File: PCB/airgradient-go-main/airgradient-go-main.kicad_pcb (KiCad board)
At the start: 4 copper layers, 62.9 x 88.3 mm, 192 parts, among them CN3 SM05B-SRSS-TB (LF)(SN), CN4 SM05B-SRSS-TB (LF)(SN), CN5 SM05B-SRSS-TB (LF)(SN), Q1 SIA445EDJ-T1-GE3, Q2 ZVN4106FTA_C508255, Q3 CSD83325L, Q4 SS8050-G, Q5 SI1308EDL, SW1 TS-1091C-A1B3-D2, SW2 TS-1091C-A1B3-D2, U1 W25N512GVEIG, U10 SGP41-D-R4, U11 PS1-CO-SMOKE-10k, U12 SHT4x, U13 SPL07-003, U14 LIS2DH12TR, U15 TMUX121NKGR_C22428404, U16 S12, U17 TCA6408ARGT, U18 TAU1113, U19 LM66200DRLR, U2 ZDSD512MLGEAG, U20 LP5036, U3 BQ27742YZFR-G1, U4 ESP32-C5-MINI-1, U5 BQ25628RYKR, U6 HYG-8503A, U7 TPL5010DDCR, U8 TPS63802DLAR, U9 TPS7A0228DQNR

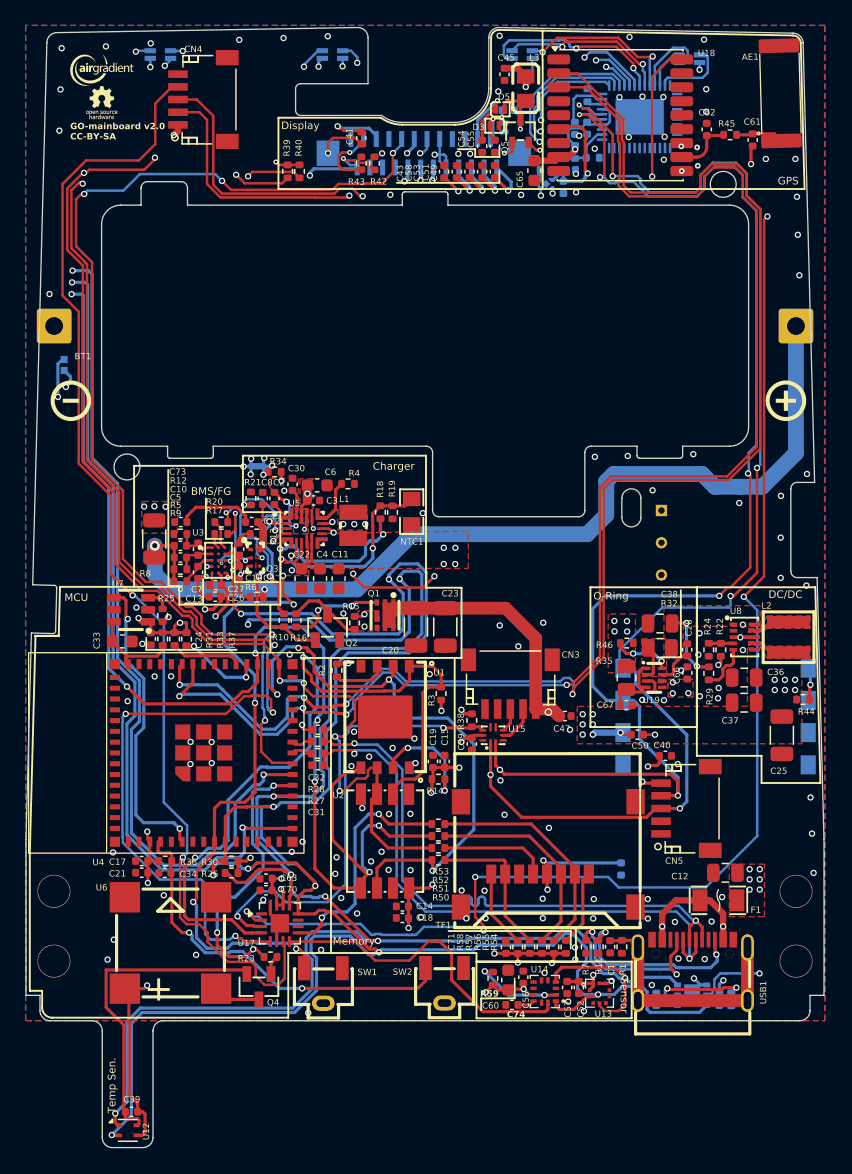
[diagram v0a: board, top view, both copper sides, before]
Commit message: Schematic: - Change SPI pull-ups R2/R3/R14 from 10K to 100K - Connect C74 decoupling cap to +3.1V rail (was floating)
PCB:
- Narrow the board outline around the temperature sensor area
- Move S12 0.3mm left and rework nearby I2C tracks
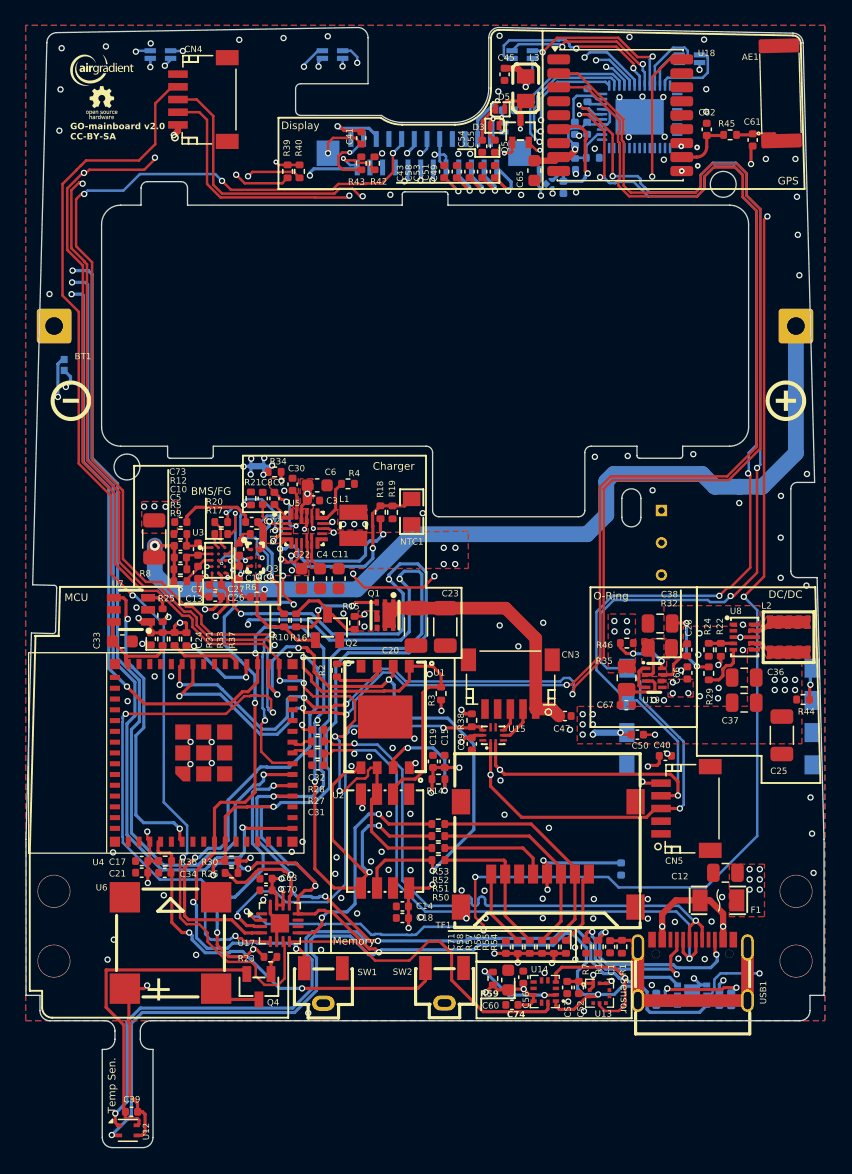
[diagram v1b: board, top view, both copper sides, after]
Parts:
- R14, R2, R3: value 10K -> 100K
- moved U16 0.30 mm to (155.6, 102.5)
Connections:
- C74 pad 2: Net-(U14-VDD_IO) -> +3.1V
- U14 pad 10: Net-(U14-VDD_IO) -> +3.1V
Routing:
- net /SCL: track 350.2 -> 353.9 mm
- net +3.1V: track 116.9 -> 118.7 mm
- net Net-(U14-VDD_IO): track 1.35 -> 0.00 mm
- net /SDA: track 341.5 -> 340.1 mm
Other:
- outline, holes or cut-outs redrawn

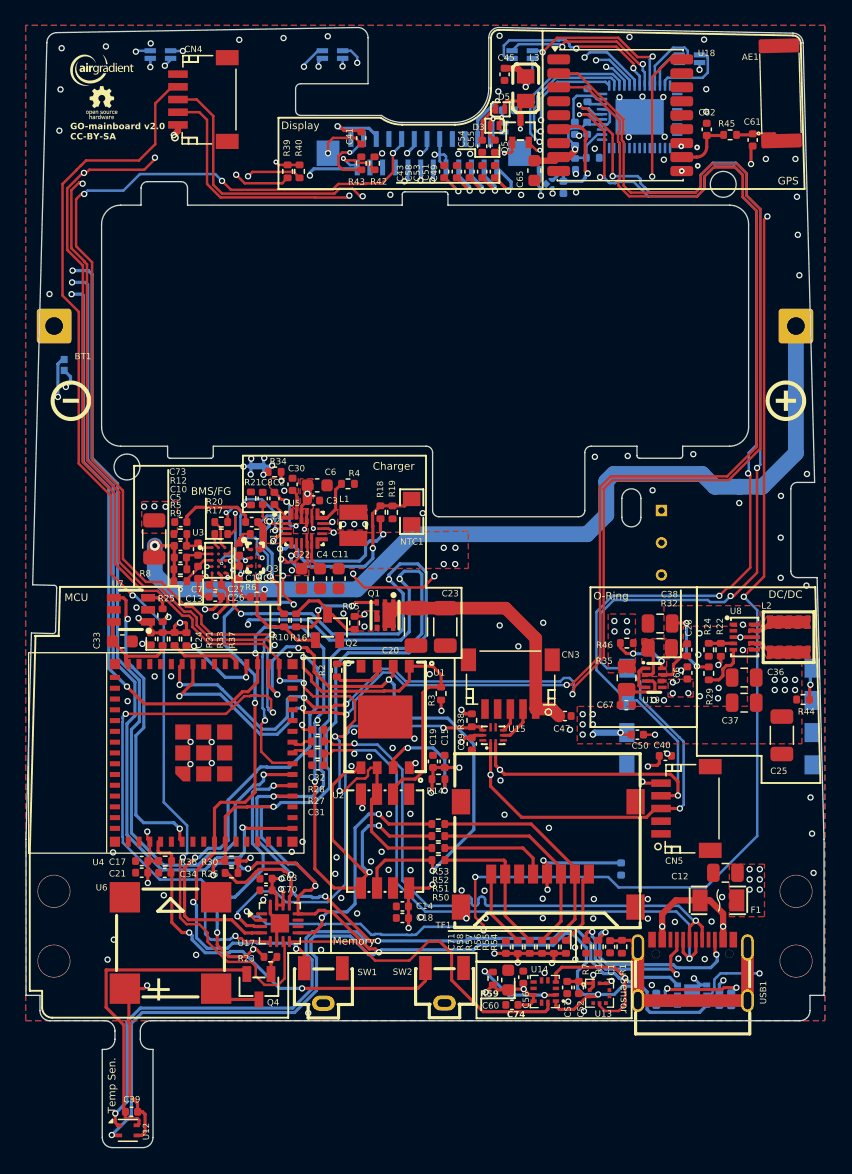
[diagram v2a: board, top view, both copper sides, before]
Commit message: v2.1: post-prototype fixes from v2.0 review and issue #1
- Battery: add C75 (100nF 0402) from BAT+ to GND at the battery +
  terminal as an RF shunt, with a GND via next to it
- NTC1 moved next to the battery negative tab (B.Cu), part changed
  to NCP15XH103F03RC; BQ25628 TS divider R18/R19 = 5.23k/30.1k
- Add R60 100K pull-up on TCA6408 RESET
- BOM: fix LCSC part numbers that were shared across different values
  (R13 2K -> C4109, R5/R12 200R -> C25087, 100K group -> C60491,
  C17/C21/C27 corrected)
- Remove test point footprints that were placed outside the board
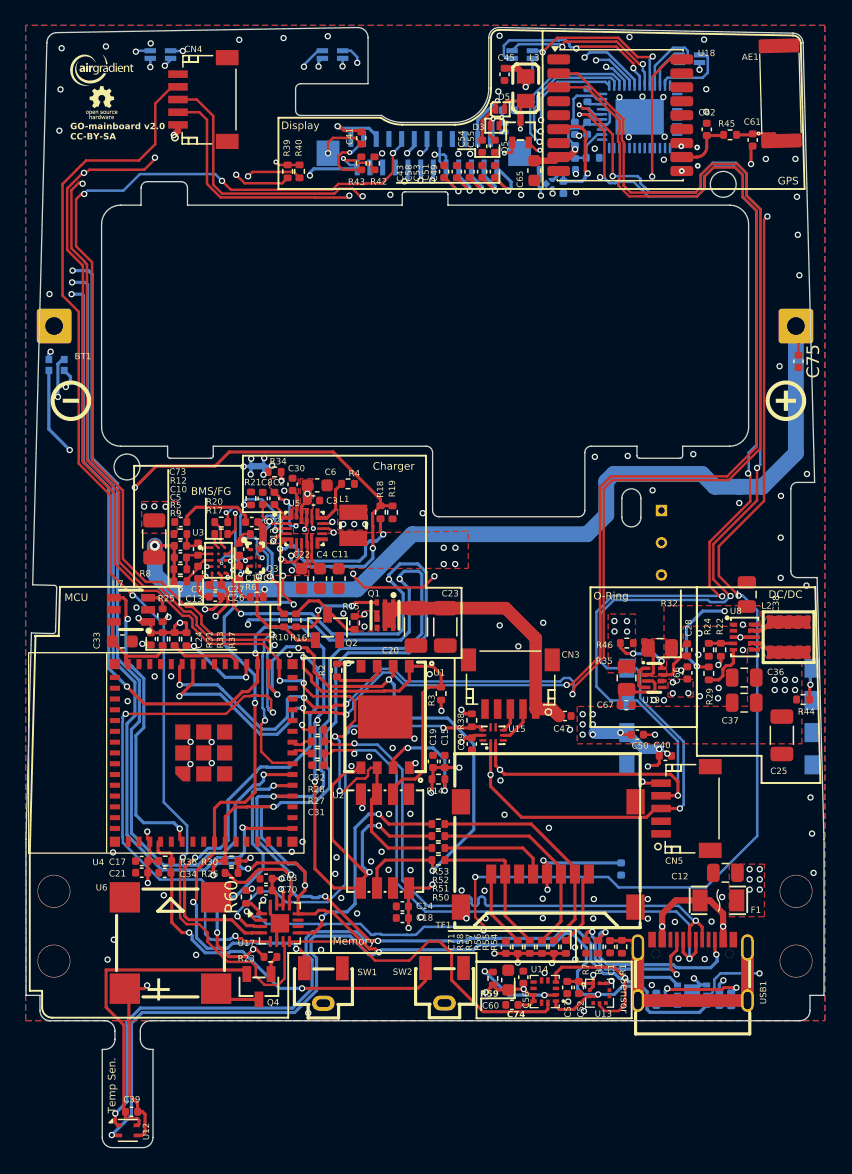
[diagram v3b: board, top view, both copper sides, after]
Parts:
- added C75: 0.1uF/25V, Capacitor_SMD:C_0402_1005Metric, F.Cu at (161.4, 85.1)
- added R60: 100K, Resistor_SMD:R_0402_1005Metric, F.Cu at (117.9, 127.3)
- NTC1: value KNTC0805/10KF3950 -> NCP15XH103F03RC; footprint easyeda2kicad-oaf:R0805 -> easyeda2kicad-oaf:R0402; moved to B.Cu
- R18: value 4.12K -> 5.23k
- R19: value 17.33K -> 30.1k
- moved NTC1 30.8 mm to (102.3, 85.4)
- moved C38 7.21 mm to (157.3, 103.5), turned to -90 degrees
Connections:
- NTC1 pad 1: GND -> Net-(U5-TS)
- NTC1 pad 2: Net-(U5-TS) -> GND
- U17 pad 1: unconnected-(U17-~{RESET}-Pad1) -> Net-(U17-~{RESET})
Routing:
- net Net-(U5-TS): track 15.7 -> 50.6 mm, vias 2 -> 4
- net GND: track 46.5 -> 54.5 mm, vias 145 -> 147
- net +3.1V: track 118.7 -> 122.3 mm, vias 51 -> 53
- net /BAT+: track 76.9 -> 79.3 mm
- net Net-(U8-EN): track 5.86 -> 7.91 mm
- net /PRTRG: track 124.8 -> 126.6 mm
- net /SDA: track 340.1 -> 341.9 mm
- net Net-(U17-~{RESET}): track 0.00 -> 1.55 mm

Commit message: Bump board revision to 2.1 (title block, silkscreen)
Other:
- board text added: "GO-mainboard v2.1 CC-BY-SA"
- board text removed: "GO-mainboard v2.0 CC-BY-SA"
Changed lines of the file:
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@@
 	(title_block
 		(title "Airgradient-GO")
-		(date "2026-05-13")
-		(rev "2.0")
+		(date "2026-09-23")
+		(rev "2.1")
 		(company "Airgradient")
 		(comment 1 "CC-BY-SA")
@@
 		(layer "User.1")
 	)
-	(gr_text "GO-mainboard v2.0\nCC-BY-SA"
+	(gr_text "GO-mainboard v2.1\nCC-BY-SA"
 		(at 103.991466 67.67 0)
 		(layer "F.SilkS")
